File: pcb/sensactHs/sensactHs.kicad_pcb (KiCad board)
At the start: 2 copper layers, 100 x 86.5 mm, 311 parts, among them M1 Hole, M2 Hole, P1 USB, P2 SWD, P3 2, P4 1, P5 3, P6 CONN_01X04, Q1 Q_NPN_BEC, SW2 BOOT0, SW3 RESET, U1 PCA9555, U10 SRV05, U11 SRV05, U12 SRV05, U13 SRV05, U14 SRV05, U15 SRV05, U16 SRV05, U17 SRV05, U18 SRV05, U19 SRV05, U2 PCA9555, U20 SRV05, U21 DRV8860woPad, U22 DRV8860woPad, U23 DRV8860woPad, U24 ULN2803, U25 PCA9685, U26 STM32F103RG, U27 LM2674, U28 SN65HVD230, U29 DS2482, U3 PCA9555, U30 DS2482, U31 DRV8860woPad, U32 DRV8860woPad, U33 DRV8860woPad, U4 PCA9555, U5 SRV05, U6 SRV05, U7 SRV05, U8 SRV05, U9 SRV05, X1 CRYSTAL_SMD_4pol

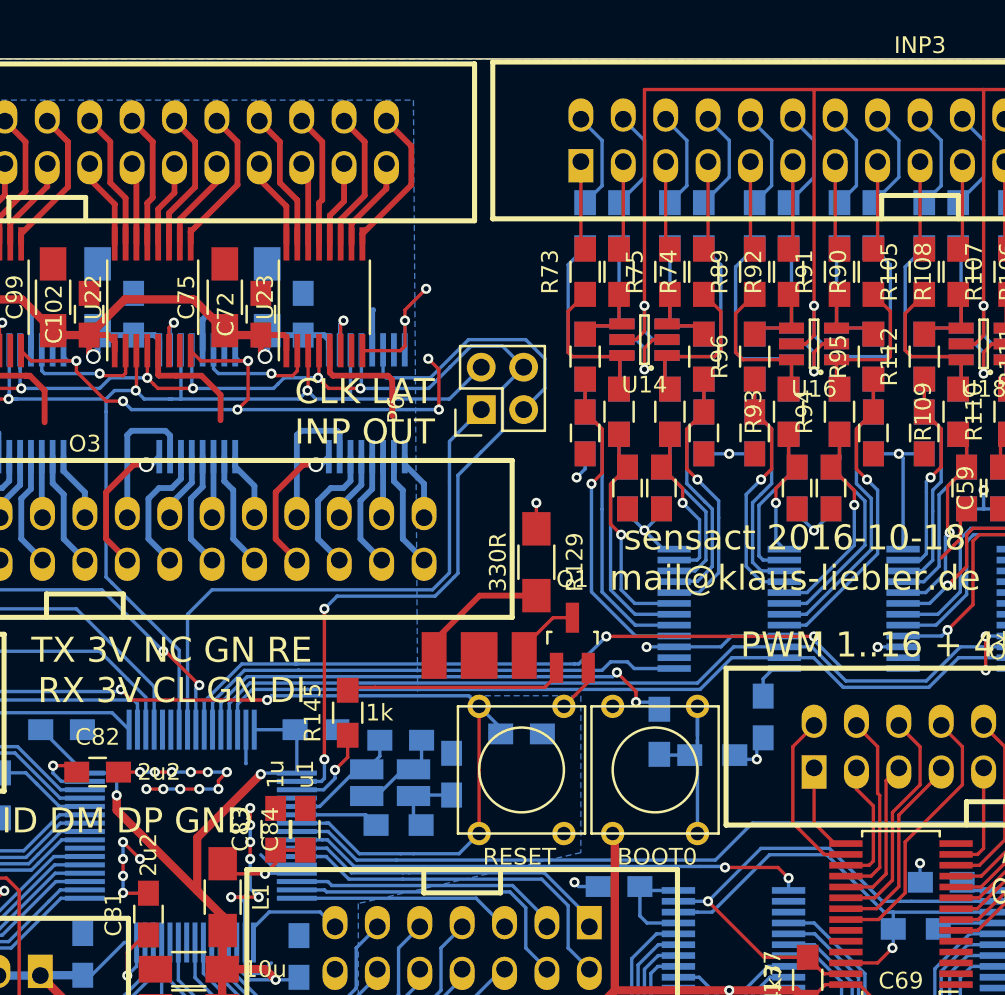
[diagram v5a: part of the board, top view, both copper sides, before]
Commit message: Added VBAT-Standby
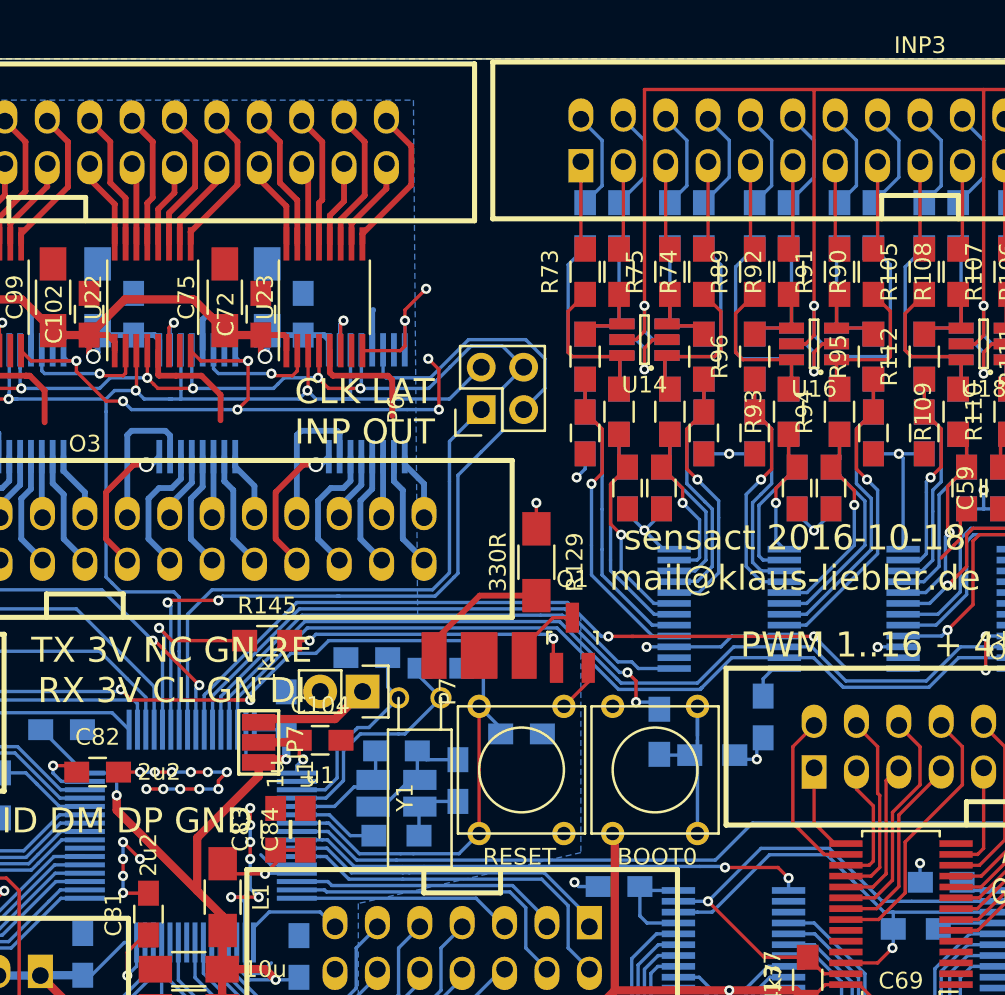
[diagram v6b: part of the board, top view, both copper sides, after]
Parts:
- added C104: u1, Capacitors_SMD:C_0805_HandSoldering, F.Cu at (61.8, 60.3)
- added C70: 10p, Capacitors_SMD:C_0805_HandSoldering, B.Cu at (64.6, 55.4)
- added C71: 10p, Capacitors_SMD:C_0805_HandSoldering, B.Cu at (69.1, 56.0)
- added JP7: JUMPER3, sensact:SMD-solder-bridge-3pin, F.Cu at (58.2, 60.5)
- added P7: CONN_01X02, Pin_Headers:Pin_Header_Straight_1x02, F.Cu at (64.4, 57.4)
- added Y1: Crystal_Small, Crystals:Crystal_Watch, F.Cu at (67.8, 57.8)
- moved R145 6.48 mm to (58.7, 54.4), turned to 0 degrees
- moved C86 2.05 mm to (59.8, 58.7), turned to 90 degrees
- moved X1 0.74 mm to (66.4, 63.5)
- moved C78 0.68 mm to (66.4, 61.0)
- moved R135 0.65 mm to (66.4, 66.0)
- moved C79 0.54 mm to (70.1, 62.7)
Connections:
- P6 pad 4: /02 output/PC13 -> LAT
- R145 pad 1: /03 cpu/PC14 -> /03 cpu/PC12
- U21 pad 4: /02 output/PC13 -> LAT
- U22 pad 4: /02 output/PC13 -> LAT
- U23 pad 4: /02 output/PC13 -> LAT
- U26 pad 1: +3V3 -> Net-(C104-Pad1)
- U26 pad 2: /02 output/PC13 -> (no net)
- U26 pad 4: (no net) -> /03 cpu/PC15
- U26 pad 53: (no net) -> /03 cpu/PC12
- U26 pad 54: (no net) -> LAT
- U31 pad 4: /02 output/PC13 -> LAT
- U32 pad 4: /02 output/PC13 -> LAT
- U33 pad 4: /02 output/PC13 -> LAT
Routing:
- net LAT: track 0.00 -> 88.7 mm, vias 0 -> 7
- net /02 output/PC13: track 83.5 -> 0.00 mm, vias 7 -> 0
- net /03 cpu/PC15: track 0.00 -> 14.5 mm
- net /03 cpu/PC12: track 0.00 -> 11.7 mm, vias 0 -> 1
- net /03 cpu/PC14: track 5.47 -> 12.5 mm, vias 1 -> 0
- net Net-(JP7-Pad1): track 0.00 -> 6.99 mm
- net /NRST: track 56.5 -> 61.8 mm
- net Net-(C104-Pad1): track 0.00 -> 4.71 mm, vias 0 -> 1
- net Net-(Q1-Pad1): track 13.3 -> 17.9 mm, vias 0 -> 2
- net Net-(R134-Pad1): track 29.9 -> 33.4 mm
- net SDA1: track 111.9 -> 115.3 mm
- net SCL1: track 115.9 -> 119.2 mm
- net /01 input/PB7: track 30.5 -> 33.3 mm
- net GND: track 238.2 -> 240.6 mm
- net SCK1: track 70.8 -> 72.7 mm
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
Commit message: PCB Update
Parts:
- moved C71 1.28 mm to (70.4, 56.1)
- moved L2 0.51 mm to (71.1, 84.1)
- moved C79 0.18 mm to (70.0, 62.6)
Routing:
- net GND: track 240.6 -> 232.7 mm
- net /NRST: track 61.8 -> 64.6 mm
- net +3V3: track 462.2 -> 459.8 mm
- net Net-(R116-Pad1): track 17.2 -> 18.3 mm
- net /03 cpu/PC14: track 12.5 -> 13.2 mm

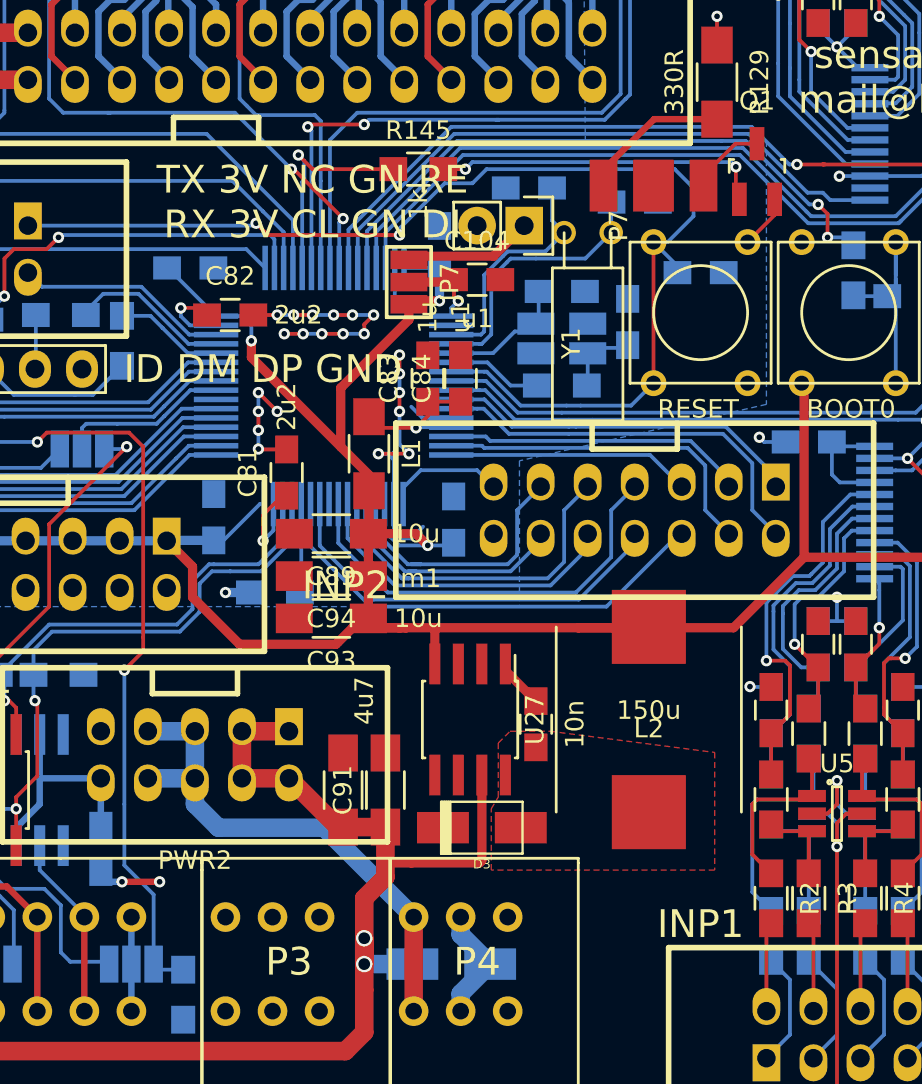
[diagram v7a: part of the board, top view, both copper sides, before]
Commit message: Merged PCB (manually)
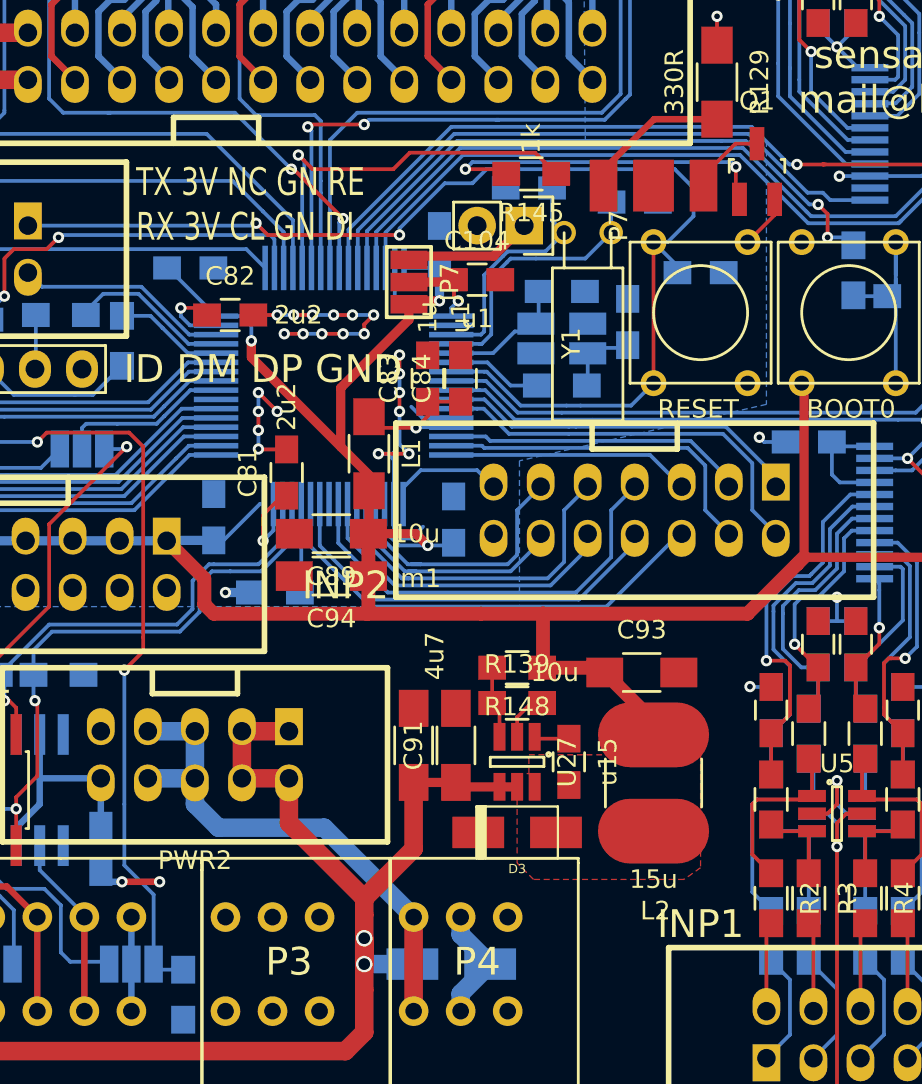
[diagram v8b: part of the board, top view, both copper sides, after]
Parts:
- added R139: 1k, Resistors_SMD:R_0805_HandSoldering, F.Cu at (64.0, 83.2)
- added R148: 3k3, Resistors_SMD:R_0805_HandSoldering, F.Cu at (64.0, 81.3)
- C90: value 10n -> u15
- L2: value 150u -> 15u; footprint sensact:Inductor_CD104_handsolder -> sensact:CD54
- U27: value LM2674 -> LMR14006; footprint sensact:SOIC-8_3.9x4.9mm_Pitch1.27mm_handsolder -> sensact:SOT-23-6_handsolder
- moved C93 17.0 mm to (70.7, 81.5), turned to 0 degrees
- moved R145 6.10 mm to (64.8, 54.6), turned to 180 degrees
- moved C91 4.51 mm to (60.7, 85.5)
- moved C92 4.51 mm to (58.4, 85.5)
- moved L2 3.44 mm to (71.4, 87.5), turned to 180 degrees
- moved U27 3.42 mm to (64.0, 86.4)
- moved C90 2.70 mm to (66.8, 86.4)
- moved D3 1.92 mm to (64.0, 90.2)
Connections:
- M1 pad 1: (no net) -> Net-(M1-Pad1)
- M2 pad 1: (no net) -> Net-(M2-Pad1)
- P2 pad 5: (no net) -> Net-(P2-Pad5)
- U21 pad 7: (no net) -> Net-(U21-Pad7)
- U22 pad 7: (no net) -> Net-(U22-Pad7)
- U23 pad 7: (no net) -> Net-(U23-Pad7)
- U25 pad 25: (no net) -> Net-(U25-Pad25)
- U26 pad 2: (no net) -> /03 cpu/PC13
- U26 pad 25: (no net) -> /03 cpu/PC5
- U26 pad 39: (no net) -> /03 cpu/PC8
- U27 pad 3: GND -> Net-(R139-Pad1)
- U27 pad 4: +3V3 -> +24V
- U27 pad 5: (no net) -> +24V
- U27 pad 6: GND -> /04 power/V_SW
- U28 pad 5: (no net) -> Net-(U28-Pad5)
- U29 pad 6: (no net) -> Net-(U29-Pad6)
- U30 pad 6: (no net) -> Net-(U30-Pad6)
- U31 pad 7: (no net) -> Net-(U31-Pad7)
- U32 pad 7: (no net) -> Net-(U32-Pad7)
- U33 pad 7: (no net) -> Net-(U33-Pad7)
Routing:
- net /03 cpu/PC12: track 11.7 -> 21.4 mm
- net Net-(R139-Pad1): track 0.00 -> 3.90 mm
- net GND: track 232.7 -> 235.4 mm
- net +24V: track 259.7 -> 261.2 mm
- net Net-(Q1-Pad1): track 17.9 -> 19.0 mm
- net /04 power/V_CB: track 2.69 -> 1.89 mm
